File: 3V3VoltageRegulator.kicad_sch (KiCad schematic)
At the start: 3 parts, among them IC2 LD1117V33C

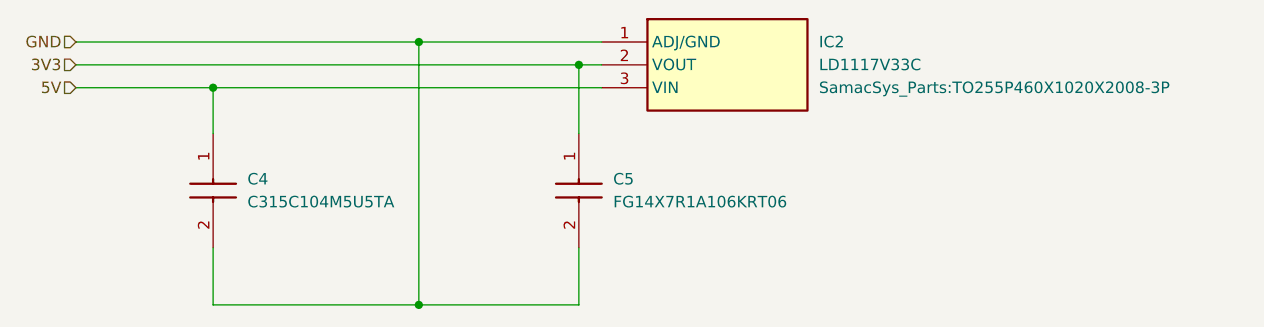
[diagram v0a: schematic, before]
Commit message: Swapped components for those in custom library, updated labelling on PCB.
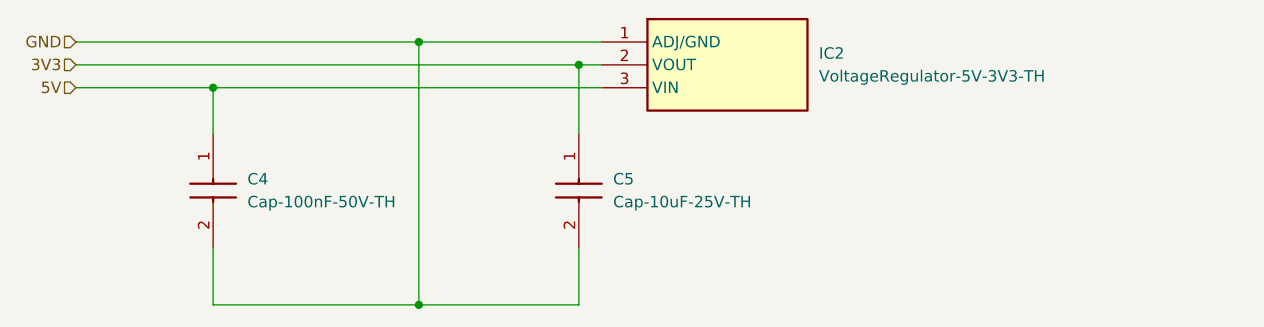
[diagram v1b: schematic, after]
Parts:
- C4: value C315C104M5U5TA -> Cap-100nF-50V-TH; footprint SamacSys_Parts:C315C100J2G5TA -> Custom:80-C315C104M5U; symbol SamacSys_Parts:C315C104M5U5TA -> Custom:Cap-100nF-50V-TH; Supplier (none) -> Mouser; Supplier Part Number (none) -> 80-C315C104M5U; Supplier Price/Stock (none) -> https://www.mouser.co.uk/ProductDetail/KEMET/C315C104M5U5TA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
- C5: value FG14X7R1A106KRT06 -> Cap-10uF-25V-TH; footprint SamacSys_Parts:FG14 -> Custom:810-FG16X7R1E106KRT6; symbol SamacSys_Parts:FG14X7R1A106KRT06 -> Custom:Cap-10uF-25V-TH; Manufacturer_Part_Number FG14X7R1A106KRT06 -> FG16X7R1E106KRT06; Supplier (none) -> Mouser; Supplier Part Number (none) -> 810-FG16X7R1E106KRT6; Supplier Price/Stock (none) -> https://www.mouser.co.uk/ProductDetail/TDK/FG16X7R1E106KRT0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
- IC2: value LD1117V33C -> VoltageRegulator-5V-3V3-TH; footprint SamacSys_Parts:TO255P460X1020X2008-3P -> Custom:511-LD1117V33C; symbol SamacSys_Parts:LD1117V33C -> Custom:VoltageRegulator-5V-3V3-TH; Supplier (none) -> Mouser; Supplier Part Number (none) -> 511-LD1117V33C; Supplier Price/Stock (none) -> https://www.mouser.co.uk/ProductDetail/STMicroelectronics/L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
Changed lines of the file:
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@@
 	)
 	(symbol
-		(lib_id "SamacSys_Parts:C315C104M5U5TA")
+		(lib_id "Custom:Cap-100nF-50V-TH")
 		(at 129.54 88.9 270)
 		(unit 1)
@@
 			)
 		)
-		(property "Value" "C315C104M5U5TA"
+		(property "Value" "Cap-100nF-50V-TH"
 			(at 133.35 96.5199 90)
 			(effects
@@
 			)
 		)
-		(property "Footprint" "SamacSys_Parts:C315C100J2G5TA"
+		(property "Footprint" "Custom:80-C315C104M5U"
 			(at 33.35 97.79 0)
 			(effects
@@
 		(property "Manufacturer_Part_Number" "C315C104M5U5TA"
 			(at -666.65 97.79 0)
+			(effects
+				(font
+					(size 1.27 1.27)
+				)
+				(justify left top)
+				(hide yes)
+			)
+		)
+		(property "Supplier" "Mouser"
+			(at 129.54 88.9 0)
+			(effects
+				(font
+					(size 1.27 1.27)
+				)
+				(hide yes)
+			)
+		)
+		(property "Supplier Part Number" "80-C315C104M5U"
+			(at -366.65 97.79 0)
+			(effects
+				(font
+					(size 1.27 1.27)
+				)
+				(justify left top)
+				(hide yes)
+			)
+		)
+		(property "Supplier Price/Stock" "https://www.mouser.co.uk/ProductDetail/KEMET/C315C104M5U5TA?qs=yPUL72EuMSdlpklLgkTxlg%3D%3D"
+			(at -466.65 97.79 0)
 			(effects
 				(font
@@
 	)
 	(symbol
-		(lib_id "SamacSys_Parts:FG14X7R1A106KRT06")
+		(lib_id "Custom:Cap-10uF-25V-TH")
 		(at 170.18 88.9 270)
 		(unit 1)
@@
 			)
 		)
-		(property "Value" "FG14X7R1A106KRT06"
+		(property "Value" "Cap-10uF-25V-TH"
 			(at 173.99 96.5199 90)
 			(effects
@@
 			)
 		)
-		(property "Footprint" "SamacSys_Parts:FG14"
+		(property "Footprint" "Custom:810-FG16X7R1E106KRT6"
 			(at 73.99 97.79 0)
 			(effects
@@
 			)
 		)
-		(property "Description" "Capacitor - MLCC with Dipped Radial Lead, Capacitance=10uF, LxWxT:4.5x5.5x3mm, Lead pitch:2.5mm"
+		(property "Description" "Capacitor - MLCC with Dipped Radial Lead, Capacitance=10?F, LxWxT:5.5x6x3.5mm, Lead pitch:2.5mm"
 			(at 170.18 88.9 0)
 			(effects
@@
 			)
 		)
-		(property "Manufacturer_Part_Number" "FG14X7R1A106KRT06"
+		(property "Manufacturer_Part_Number" "FG16X7R1E106KRT06"
 			(at -626.01 97.79 0)
+			(effects
+				(font
+					(size 1.27 1.27)
+				)
+				(justify left top)
+				(hide yes)
+			)
+		)
+		(property "Supplier" "Mouser"
+			(at 170.18 88.9 0)
+			(effects
+				(font
+					(size 1.27 1.27)
+				)
+				(hide yes)
+			)
+		)
+		(property "Supplier Part Number" "810-FG16X7R1E106KRT6"
+			(at -326.01 97.79 0)
+			(effects
+				(font
+					(size 1.27 1.27)
+				)
+				(justify left top)
+				(hide yes)
+			)
+		)
+		(property "Supplier Price/Stock" "https://www.mouser.co.uk/ProductDetail/TDK/FG16X7R1E106KRT06?qs=qf2ddTMq67V1hYQaidv4ew%3D%3D"
+			(at -426.01 97.79 0)
 			(effects
 				(font
@@
 	)
 	(symbol
-		(lib_id "SamacSys_Parts:LD1117V33C")
+		(lib_id "Custom:VoltageRegulator-5V-3V3-TH")
 		(at 172.72 78.74 0)
 		(unit 1)
@@
 		(fields_autoplaced yes)
 		(property "Reference" "IC2"
-			(at 196.85 78.7399 0)
-			(effects
-				(font
-					(size 1.27 1.27)
-				)
-				(justify left)
-			)
-		)
-		(property "Value" "LD1117V33C"
-			(at 196.85 81.2799 0)
-			(effects
-				(font
-					(size 1.27 1.27)
-				)
-				(justify left)
-			)
-		)
-		(property "Footprint" "SamacSys_Parts:TO255P460X1020X2008-3P"
-			(at 196.85 83.8199 0)
-			(effects
-				(font
-					(size 1.27 1.27)
-				)
-				(justify left)
+			(at 196.85 80.0099 0)
+			(effects
+				(font
+					(size 1.27 1.27)
+				)
+				(justify left)
+			)
+		)
+		(property "Value" "VoltageRegulator-5V-3V3-TH"
+			(at 196.85 82.5499 0)
+			(effects
+				(font
+					(size 1.27 1.27)
+				)
+				(justify left)
+			)
+		)
+		(property "Footprint" "Custom:511-LD1117V33C"
+			(at 198.628 77.724 0)
+			(effects
+				(font
+					(size 1.27 1.27)
+				)
+				(justify left top)
+				(hide yes)
 			)
 		)
@@
 			)
 		)
-		(property "Description" "Voltage Regulator - LDO Regulator 3.3V 1.3A TO220 LD1117V33C, Low Dropout Voltage Regulator, 1.3A, 3.3 V +/-1%, 3-Pin TO-220"
+		(property "Description" "IC - Voltage Regulator - LDO Regulator 3.3V 1.3A TO220 LD1117V33C, Low Dropout Voltage Regulator, 1.3A, 3.3 V +/-1%, 3-Pin TO-220"
 			(at 172.72 78.74 0)
 			(effects
@@
 			(effects
 				(font
+					(size 1.27 1.27)
+				)
+				(justify left top)
+				(hide yes)
+			)
+		)
+		(property "Supplier" "Mouser"
+			(at 172.72 78.74 0)
+			(effects
+				(font
+					(size 1.27 1.27)
+				)
+				(hide yes)
+			)
+		)
+		(property "Supplier Part Number" "511-LD1117V33C"
+			(at 196.85 573.66 0)
+			(effects
+				(font
+					(size 1.27 1.27)
+				)
+				(justify left top)
+				(hide yes)
+			)
+		)
+		(property "Supplier Price/Stock" "https://www.mouser.co.uk/ProductDetail/STMicroelectronics/LD1117V33C?qs=Au9%252BK7QVGzXPdUO4sOqOiQ%3D%3D"
+			(at 196.85 673.66 0)
+			(effects
+				(font

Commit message: Updates look good, promoted to v1.2.
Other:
- title: 3.3V Voltage Regulator -> Arduino Mega CMRI WiFi Shield
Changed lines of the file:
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@@
 	(paper "A4")
 	(title_block
-		(title "3.3V Voltage Regulator")
-		(date "2026-01-30")
-		(rev "1.1")
+		(title "Arduino Mega CMRI WiFi Shield")
+		(date "2026-02-10")
+		(rev "1.2")
 	)
 	(junction
